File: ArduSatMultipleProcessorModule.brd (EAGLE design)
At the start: 95.5 x 90.3 mm, 95 parts, among them IC1 ATMEGA328P, IC2 ATMEGA328P, IC3 ATMEGA328P, IC4 ATMEGA328P, IC5 MCP23017SO, IC6 MCP23017SO, IC7 ATMEGA328P, P1 N1_ICSP, P2 N0_ICSP, P3 N0_ICSP, P4 N1_ICSP, P5 N1_ICSP, Q1 BSS138 N-MOSFET, Q10 2N7002 N-MOSFET, Q2 BSS138 N-MOSFET, Q3 BSS138 N-MOSFET, Q4 BSS138 N-MOSFET, Q5 BSS138 N-MOSFET, Q6 BSS138 N-MOSFET, Q7 BSS138 N-MOSFET, Q8 BSS138 N-MOSFET, Q9 2N7002 N-MOSFET, U1 MUX-74HC4067, U2 MUX-74HC4067, U3 MUX-74HC4067, U4 MUX-74HC4067

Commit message: Supervisor now has control of both node power and serial comms
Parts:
- removed U1, U2, U3, U4: MUX-74HC4067, SparkFun:SSOP24
- added IC8: MCP23S17ML, freetronics-jon:QFN28-ML_6X6MM
- added U$57, U$58, U$59, U$60: MUX-74HC4067-QFNSMT, freetronics-jon:DHVQFN24
- IC5, IC6: value MCP23017SO -> MCP23017ML; device microchip:SO28W -> freetronics-jon:QFN28-ML_6X6MM
- moved C15 293.1 mm to (65.4, 48.9)
- moved JP3 293.1 mm to (69.2, 55.9)
- moved Q10 293.1 mm to (65.4, 52.1)
- moved Q9 293.1 mm to (65.4, 56.5)
- moved C13 238.7 mm to (36.8, 31.1)
- moved C14 238.7 mm to (41.3, 31.1)
- moved IC7 238.7 mm to (38.7, 47.6)
- moved JP2 238.7 mm to (40.0, 57.8)
- moved P5 238.7 mm to (40.0, 37.5)
- moved R20 238.7 mm to (45.7, 61.6)
- moved R22 238.7 mm to (48.9, 61.6)
- moved R23 238.7 mm to (52.1, 61.6)
- moved R24 238.7 mm to (55.2, 61.6)
- moved R25 238.7 mm to (36.8, 54.0)
- moved R26 238.7 mm to (45.7, 31.1)
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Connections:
- net S_D0_N2_PWR renamed S_D0
- net S_D1_N3_PWR renamed S_D1
- net S_D2_N4_PWR renamed S_D2
- net S_D3_N5_PWR renamed S_D3
- net S_D4_N6_PWR renamed S_D4
- removed net N10_5V: IC6.3
- removed net N11_5V: IC6.4
- removed net N12_5V: IC6.5
- removed net N13_5V: IC6.6
- removed net N14_5V: IC6.7
- removed net N15_5V: IC6.8
- removed net N4_5V: IC6.25
- removed net N5_5V: IC6.26
- removed net N6_5V: IC6.27
- removed net N7_5V: IC6.28
- removed net N8_5V: IC6.1
- removed net N9_5V: IC6.2
- removed net S_A6_N0_PWR: IC7.19, Q9.1
- removed net S_A7_N1_PWR: IC7.22, Q10.1
- new net N$90: IC8.14
- new net N0_PWR: IC6.17, IC8.17, Q9.1
- new net N10_PWR: IC6.27, IC8.27
- new net N11_PWR: IC6.28, IC8.28
- new net N12_PWR: IC6.1, IC8.1
- new net N13_PWR: IC6.2, IC8.2
- new net N14_PWR: IC6.3, IC8.3
- new net N15_PWR: IC6.4, IC8.4
- new net N1_PWR: IC6.18, IC8.18, Q10.1
- new net N2_PWR: IC6.19, IC8.19
- new net N3_PWR: IC6.20, IC8.20
- new net N4_PWR: IC6.21, IC8.21
- new net N5_PWR: IC6.22, IC8.22
- new net N6_PWR: IC6.23, IC8.23
- new net N7_PWR: IC6.24, IC8.24
- new net N8_PWR: IC6.25, IC8.25
- new net N9_PWR: IC6.26, IC8.26
- new net S_A6: IC7.19, R33.1, U$59.15, U$60.15
- new net S_A7: IC7.22
- net +5V_SYS: now also IC5.5, IC6.5, IC8.5, R33.2, U$57.24, U$57.25, U$58.24, U$58.25, U$59.24, U$59.25, U$60.24, U$60.25; no longer IC5.9, IC6.9, U1.24, U2.24, U3.24, U4.24
- net ADDR0: now also IC5.11; no longer IC5.15
- net ADDR1: now also IC5.12; no longer IC5.16
- net ADDR2: now also IC5.13; no longer IC5.17
- net GND: now also IC5.6, IC6.6, IC8.11, IC8.12, IC8.13, IC8.6, U$57.12, U$58.12, U$59.12, U$60.12; no longer IC5.10, IC6.10, R33.1, U1.12, U2.12, U3.12, U4.12
- net N0_5V: no longer IC6.21
- net N0_D0_RX: now also U$58.9, U$59.9; no longer U2.9, U4.9
- net N0_D1_TX: now also U$57.9, U$60.9; no longer U1.9, U3.9
- net N10_D0_RX: now also U$58.21, U$59.21; no longer U2.21, U4.21
- net N10_D1_TX: now also U$57.21, U$60.21; no longer U1.21, U3.21
- net N11_D0_RX: now also U$58.20, U$59.20; no longer U2.20, U4.20
- net N11_D1_TX: now also U$57.20, U$60.20; no longer U1.20, U3.20
- net N12_D0_RX: now also U$58.19, U$59.19; no longer U2.19, U4.19
- net N12_D1_TX: now also U$57.19, U$60.19; no longer U1.19, U3.19
- net N13_D0_RX: now also U$58.18, U$59.18; no longer U2.18, U4.18
- net N13_D1_TX: now also U$57.18, U$60.18; no longer U1.18, U3.18
- net N14_D0_RX: now also U$58.17, U$59.17; no longer U2.17, U4.17
- net N14_D1_TX: now also U$57.17, U$60.17; no longer U1.17, U3.17
- net N15_D0_RX: now also U$58.16, U$59.16; no longer U2.16, U4.16
- net N15_D1_TX: now also U$57.16, U$60.16; no longer U1.16, U3.16
- net N1_5V: no longer IC6.22
- net N1_D0_RX: now also U$58.8, U$59.8; no longer U2.8, U4.8
- net N1_D1_TX: now also U$57.8, U$60.8; no longer U1.8, U3.8
- net N2_5V: no longer IC6.23
- net N2_D0_RX: now also U$58.7, U$59.7; no longer U2.7, U4.7
- net N2_D1_TX: now also U$57.7, U$60.7; no longer U1.7, U3.7
- net N3_5V: no longer IC6.24
- net N3_D0_RX: now also U$58.6, U$59.6; no longer U2.6, U4.6
- net N3_D1_TX: now also U$57.6, U$60.6; no longer U1.6, U3.6
- net N4_D0_RX: now also U$58.5, U$59.5; no longer U2.5, U4.5
- net N4_D1_TX: now also U$57.5, U$60.5; no longer U1.5, U3.5
- net N5_D0_RX: now also U$58.4, U$59.4; no longer U2.4, U4.4
- net N5_D1_TX: now also U$57.4, U$60.4; no longer U1.4, U3.4
- net N6_D0_RX: now also U$58.3, U$59.3; no longer U2.3, U4.3
- net N6_D1_TX: now also U$57.3, U$60.3; no longer U1.3, U3.3
- net N7_D0_RX: now also U$58.2, U$59.2; no longer U2.2, U4.2
- net N7_D1_TX: now also U$57.2, U$60.2; no longer U1.2, U3.2
- net N8_D0_RX: now also U$58.23, U$59.23; no longer U2.23, U4.23
- net N8_D1_TX: now also U$57.23, U$60.23; no longer U1.23, U3.23
- net N9_D0_RX: now also U$58.22, U$59.22; no longer U2.22, U4.22
- net N9_D1_TX: now also U$57.22, U$60.22; no longer U1.22, U3.22
- net PWR_ADDR0: now also IC6.11; no longer IC6.15
- net PWR_ADDR1: now also IC6.12; no longer IC6.16
- net PWR_ADDR2: now also IC6.13; no longer IC6.17
- net RESET: now also IC5.14, IC6.14; no longer IC5.18, IC6.18
- net RX: now also U$58.1, U$59.1; no longer U2.1, U4.1
- net S_A0: now also IC5.17, U$57.10, U$58.10, U$59.10, U$60.10; no longer IC5.21, U1.10, U2.10, U3.10, U4.10
- net S_A1: now also IC5.18, U$57.11, U$58.11, U$59.11, U$60.11; no longer IC5.22, U1.11, U2.11, U3.11, U4.11
- net S_A2: now also IC5.19, U$57.14, U$58.14, U$59.14, U$60.14; no longer IC5.23, U1.14, U2.14, U3.14, U4.14
- net S_A3: now also IC5.20, U$57.13, U$58.13, U$59.13, U$60.13; no longer IC5.24, U1.13, U2.13, U3.13, U4.13
- net S_A4_SDA: now also IC5.9, IC6.9; no longer IC5.13, IC6.13
- net S_A5_SCL: now also IC5.8, IC6.8; no longer IC5.12, IC6.12
- net S_D10: now also IC8.7
- net S_D11_MOSI: now also IC8.9
- net S_D12_MISO: now also IC8.10
- net S_D13_SCK: now also IC8.8
- net TX: now also U$57.1, U$60.1; no longer U1.1, U3.1
- net UART_EN: now also U$57.15, U$58.15; no longer R33.2, U1.15, U2.15, U3.15, U4.15

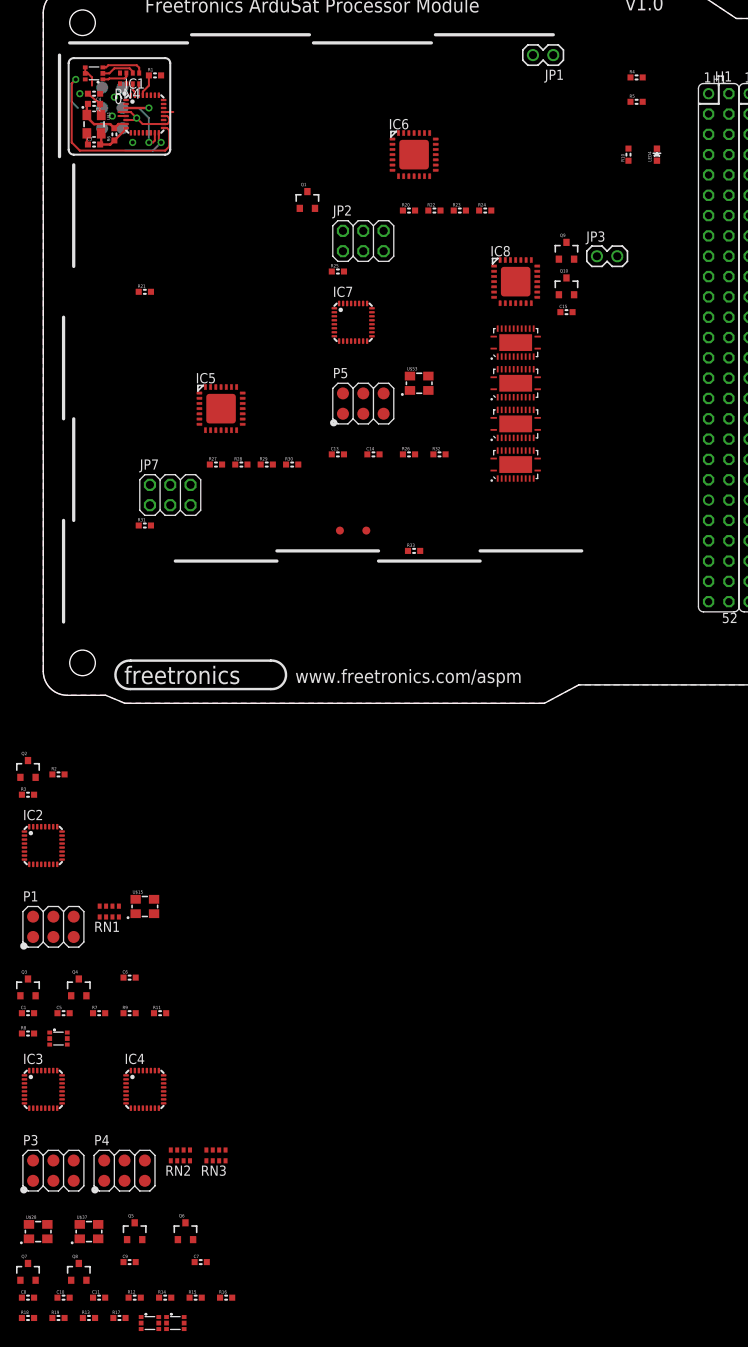
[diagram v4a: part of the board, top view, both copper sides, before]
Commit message: Removed direct control option for UART MUX and power
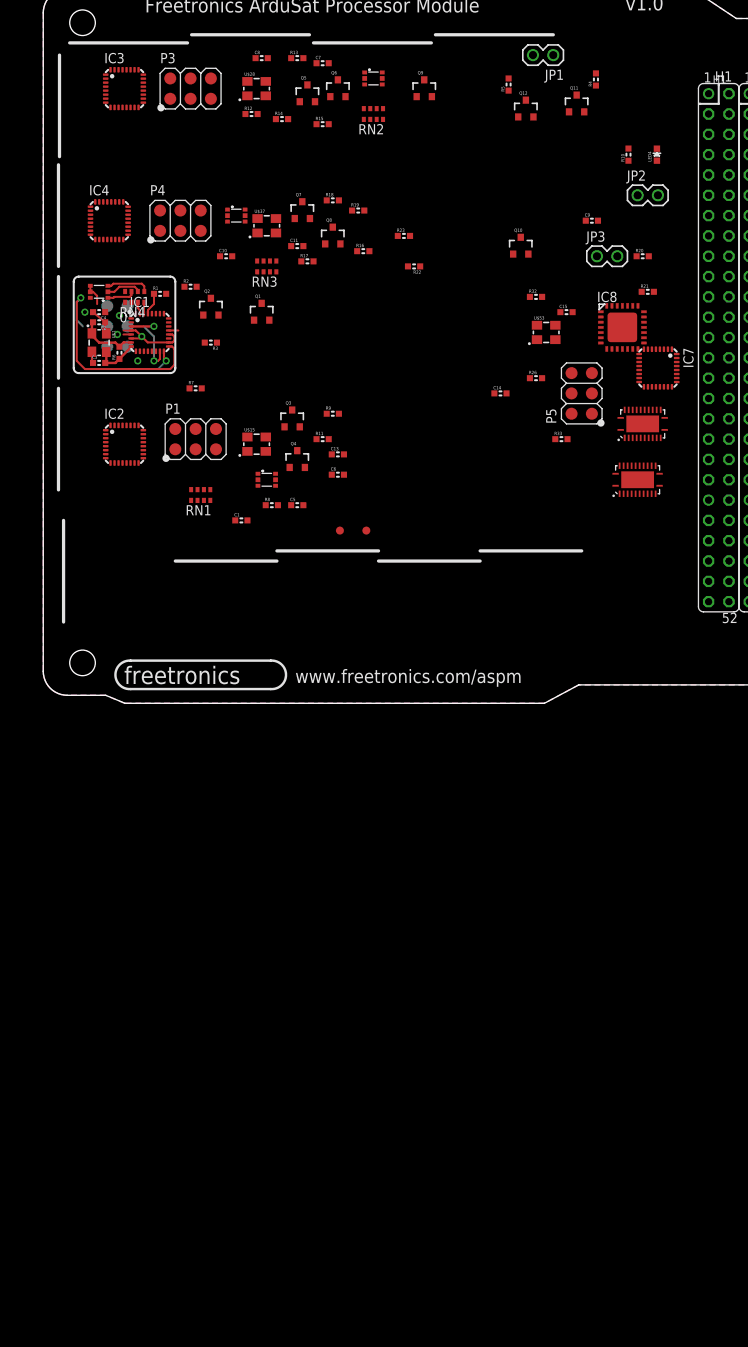
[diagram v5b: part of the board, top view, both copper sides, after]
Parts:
- removed IC5, IC6: MCP23017ML, freetronics-jon:QFN28-ML_6X6MM
- removed JP7: (no value), freetronics-master-v1.1:2X03
- removed R24, R25, R27, R28: 4K7, freetronics-master-v1:0603
- removed R29, R30, R31: 33K, freetronics-master-v1:0603
- removed U$57, U$58: MUX-74HC4067-QFNSMT, freetronics-jon:DHVQFN24
- added Q11, Q12: BSS138 N-MOSFET, freetronics-master-v1:SOT23-3
- JP2: device freetronics-master-v1.1:2X03 -> freetronics-master-v1.1:1X02
- R20: value 33K -> 100K 0603; device freetronics-master-v1:0603 -> freetronics-master-v1.1:0603
- R21: value 33K 0603 -> 100K 0603
- R22, R23: value 33K -> 10K 0603; device freetronics-master-v1:0603 -> freetronics-master-v1.1:0603
- moved R13 159.6 mm to (31.8, 80.6)
- moved U$29 158.1 mm to (41.3, 78.1)
- moved C8 157.7 mm to (27.3, 80.6)
- moved C7 150.6 mm to (34.9, 80.0)
- moved R12 148.7 mm to (26.0, 73.7)
- moved R14 148.0 mm to (29.8, 73.0)
- moved R15 147.5 mm to (34.9, 72.4)
- moved U$28 145.5 mm to (26.7, 76.8)
- moved R18 144.8 mm to (36.2, 62.9)
- moved Q6 144.1 mm to (36.8, 76.8)
- moved Q5 143.9 mm to (33.0, 76.2)
- moved R19 143.4 mm to (39.4, 61.6)
- moved C9 142.4 mm to (68.6, 60.3)
- moved U$38 138.6 mm to (24.1, 61.0)
- moved Q7 137.1 mm to (32.4, 61.6)
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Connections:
- removed net ADDR0: IC5.11, JP7.2, R29.2
- removed net ADDR1: IC5.12, JP7.4, R30.2
- removed net ADDR2: IC5.13, JP7.6, R31.2
- removed net PWR_ADDR0: IC6.11, JP2.2, R20.2
- removed net PWR_ADDR1: IC6.12, JP2.4, R22.2
- removed net PWR_ADDR2: IC6.13, JP2.6, R23.2
- removed net RESET: IC5.14, IC6.14
- removed net SCL: JP1.2, Q2.3, Q4.3, Q6.3, Q8.3, R5.1
- removed net SDA: JP1.1, Q1.3, Q3.3, Q5.3, Q7.3, R4.1
- removed net UART_EN: R21.2, U$57.15, U$58.15
- new net MGMNT_SCL: JP1.2, Q12.3, R5.1
- new net MGMNT_SDA: JP1.1, Q11.3, R4.1
- new net NODE_SCL: JP2.2, Q2.3, Q4.3, Q6.3, Q8.3, R21.1
- new net NODE_SDA: JP2.1, Q1.3, Q3.3, Q5.3, Q7.3, R20.1
- net +5V_SYS: now also R20.2, R21.2; no longer IC5.5, IC6.5, JP2.1, JP2.3, JP2.5, JP7.1, JP7.3, JP7.5, R24.2, R25.2, R27.2, R28.2, U$57.24, U$57.25, U$58.24, U$58.25
- net GND: no longer IC5.6, IC6.6, R20.1, R21.1, R22.1, R23.1, R29.1, R30.1, R31.1, U$57.12, U$58.12
- net N0_D0_RX: no longer U$58.9
- net N0_D1_TX: no longer U$57.9
- net N0_PWR: no longer IC6.17
- net N10_D0_RX: no longer U$58.21
- net N10_D1_TX: no longer U$57.21
- net N10_PWR: no longer IC6.27
- net N11_D0_RX: no longer U$58.20
- net N11_D1_TX: no longer U$57.20
- net N11_PWR: no longer IC6.28
- net N12_D0_RX: no longer U$58.19
- net N12_D1_TX: no longer U$57.19
- net N12_PWR: no longer IC6.1
- net N13_D0_RX: no longer U$58.18
- net N13_D1_TX: no longer U$57.18
- net N13_PWR: no longer IC6.2
- net N14_D0_RX: no longer U$58.17
- net N14_D1_TX: no longer U$57.17
- net N14_PWR: no longer IC6.3
- net N15_D0_RX: no longer U$58.16
- net N15_D1_TX: no longer U$57.16
- net N15_PWR: no longer IC6.4
- net N1_5V: now also Q11.1, Q12.1, R22.2, R23.2
- net N1_D0_RX: no longer U$58.8
- net N1_D1_TX: no longer U$57.8
- net N1_PWR: no longer IC6.18
- net N2_D0_RX: no longer U$58.7
- net N2_D1_TX: no longer U$57.7
- net N2_PWR: no longer IC6.19
- net N3_D0_RX: no longer U$58.6
- net N3_D1_TX: no longer U$57.6
- net N3_PWR: no longer IC6.20
- net N4_D0_RX: no longer U$58.5
- net N4_D1_TX: no longer U$57.5
- net N4_PWR: no longer IC6.21
- net N5_D0_RX: no longer U$58.4
- net N5_D1_TX: no longer U$57.4
- net N5_PWR: no longer IC6.22
- net N6_D0_RX: no longer U$58.3
- net N6_D1_TX: no longer U$57.3
- net N6_PWR: no longer IC6.23
- net N7_D0_RX: no longer U$58.2
- net N7_D1_TX: no longer U$57.2
- net N7_PWR: no longer IC6.24
- net N8_D0_RX: no longer U$58.23
- net N8_D1_TX: no longer U$57.23
- net N8_PWR: no longer IC6.25
- net N9_D0_RX: no longer U$58.22
- net N9_D1_TX: no longer U$57.22
- net N9_PWR: no longer IC6.26
- net RX: no longer U$58.1
- net S_A0: no longer IC5.17, U$57.10, U$58.10
- net S_A1: no longer IC5.18, U$57.11, U$58.11
- net S_A2: no longer IC5.19, U$57.14, U$58.14
- net S_A3: no longer IC5.20, U$57.13, U$58.13
- net S_A4_SDA: now also Q11.2, R22.1; no longer IC5.9, IC6.9, R24.1, R28.1
- net S_A5_SCL: now also Q12.2, R23.1; no longer IC5.8, IC6.8, R25.1, R27.1
- net TX: no longer U$57.1

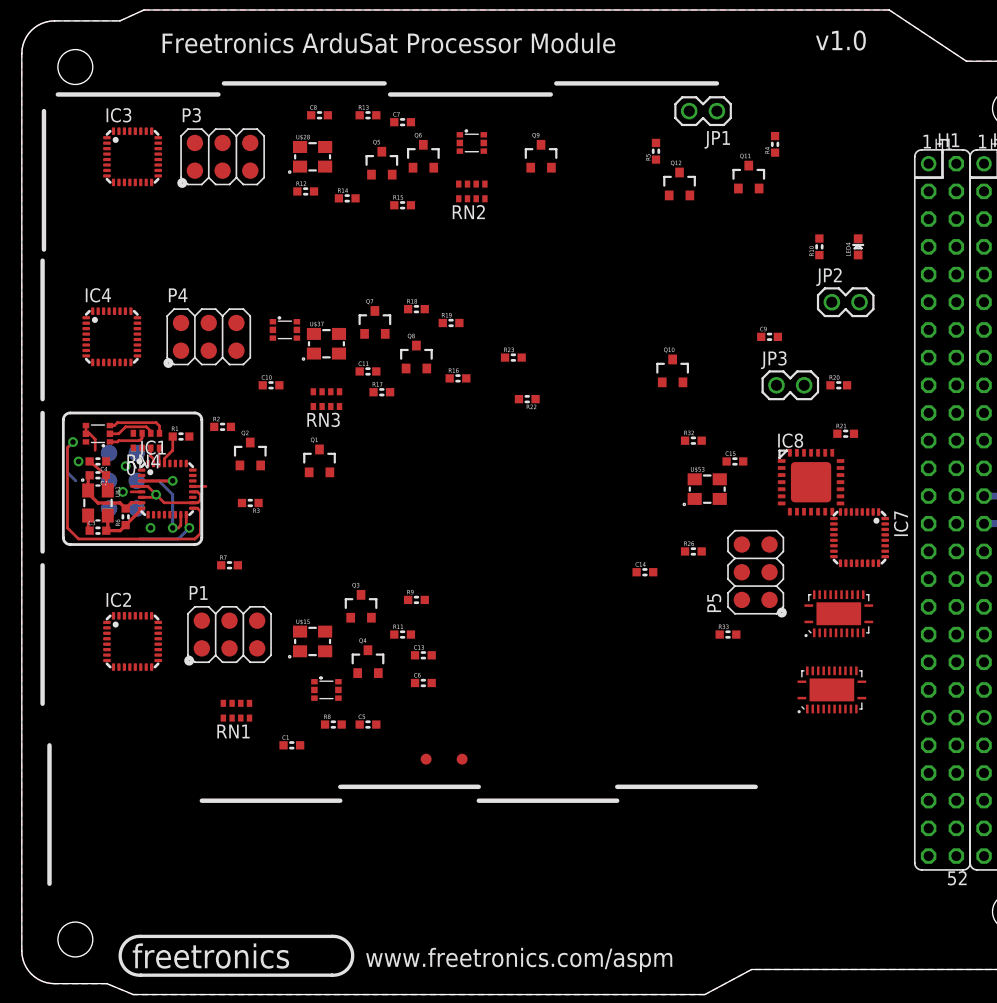
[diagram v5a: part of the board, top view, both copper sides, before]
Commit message: Experiments with node layout
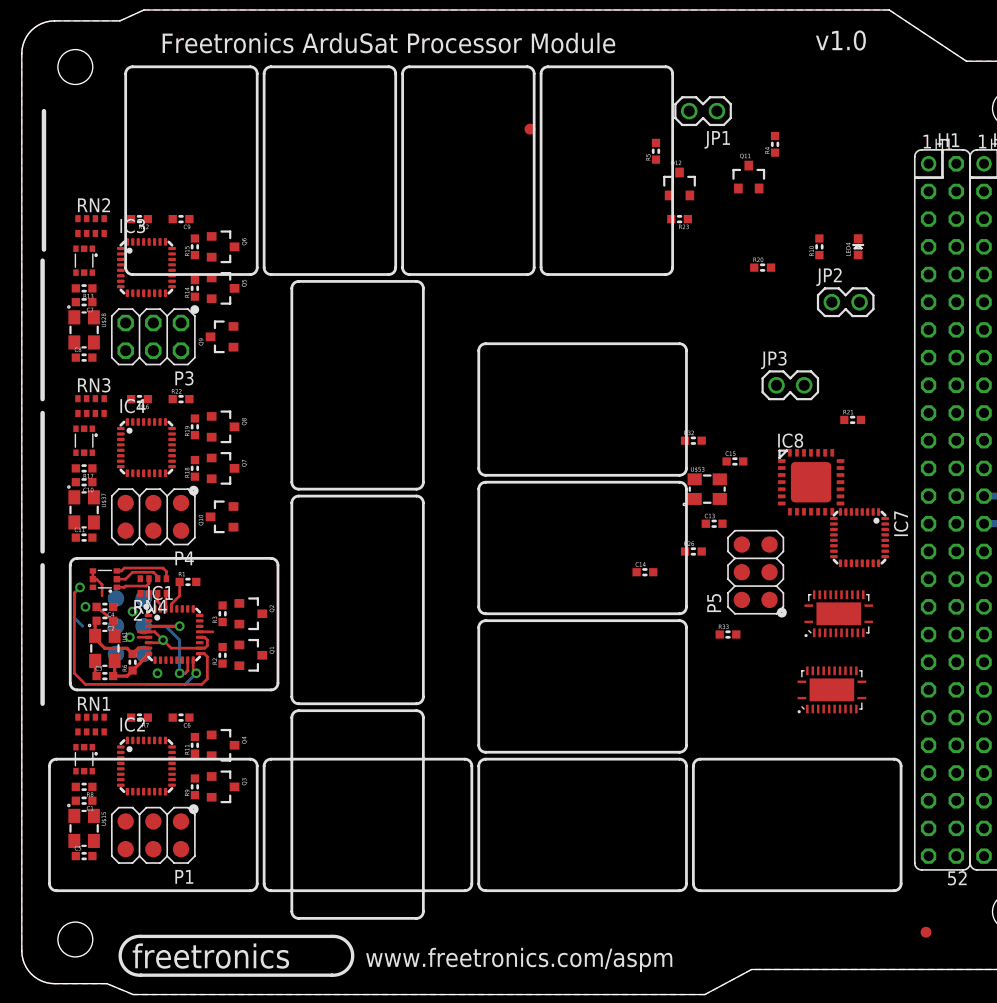
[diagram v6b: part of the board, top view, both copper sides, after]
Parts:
- P3: device freetronics-jon:2X03SURFACE -> freetronics-jon:2X03PTH
- moved U$21 58.6 mm to (46.6, 79.4)
- moved C9 55.0 mm to (14.6, 71.1), turned to 180 degrees
- moved U$22 45.4 mm to (82.9, 5.71)
- moved Q10 43.4 mm to (18.4, 43.8), turned to 90 degrees
- moved U$29 37.2 mm to (5.71, 67.3), turned to 270 degrees
- moved RN2 35.1 mm to (6.35, 70.5), turned to 180 degrees
- moved C7 33.6 mm to (5.71, 63.5), turned to 180 degrees
- moved Q9 33.6 mm to (18.4, 60.3), turned to 90 degrees
- moved R22 31.7 mm to (14.6, 54.6), turned to 0 degrees
- moved C8 31.0 mm to (5.71, 58.4)
- moved R13 30.5 mm to (5.71, 64.8), turned to 180 degrees
- moved C11 30.2 mm to (5.71, 41.9)
- moved R16 29.3 mm to (10.8, 54.6), turned to 180 degrees
- moved C13 29.3 mm to (63.5, 43.2)
- moved C5 28.7 mm to (5.71, 12.7)
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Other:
- board text added: "2"
- board text removed: "0"

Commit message: Experiments in node dimensions and layout
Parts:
- P4: device freetronics-jon:2X03SURFACE -> freetronics-jon:2X03PTH
- moved U$59 77.8 mm to (10.2, 78.1)
- moved U$60 74.6 mm to (19.7, 78.7)
- moved IC7 54.0 mm to (36.2, 77.5)
- moved IC8 53.9 mm to (27.9, 77.5)
- moved C15 46.0 mm to (19.6, 45.2)
- moved P5 42.2 mm to (52.1, 78.1)
- moved R22 41.6 mm to (52.6, 71.6), turned to 180 degrees
- moved R33 39.4 mm to (63.5, 72.4)
- moved JP2 38.6 mm to (40.0, 81.3)
- moved U$53 37.4 mm to (41.3, 76.8)
- moved C13 35.1 mm to (71.1, 77.5)
- moved C14 34.7 mm to (52.1, 73.0)
- moved R26 32.2 mm to (56.5, 72.4)
- moved JP3 31.0 mm to (43.8, 73.7)
- moved R21 27.1 mm to (71.1, 79.4)
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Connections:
- net +5V_SYS: now also Q11.1, Q12.1, R22.2, R23.2
- net GND: now also RN3.1; no longer RN3.2
- net N$19: now also U$38.3; no longer U$38.2
- net N$20: now also RN3.7, U$38.2; no longer RN3.5, U$38.3
- net N$21: now also RN3.8; no longer RN3.7
- net N1_5V: no longer Q11.1, Q12.1, R22.2, R23.2
- net N1_D0_RX: now also RN3.3; no longer RN3.4
- net N1_D1_TX: now also RN3.2; no longer RN3.3
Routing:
- net N1_5V: track 0.00 -> 42.2 mm
- net N1_D13_SCK: track 0.00 -> 17.5 mm, vias 0 -> 2
- net N1_RESET: track 0.00 -> 14.8 mm, vias 0 -> 1
- net GND: track 10.2 -> 22.9 mm, vias 5 -> 10
- net N$17: track 0.00 -> 10.8 mm
- net N1_A4_SDA: track 0.00 -> 8.53 mm
- net N$18: track 0.00 -> 8.18 mm
- net N1_A5_SCL: track 0.00 -> 7.44 mm
- net N1_D11_MOSI: track 0.00 -> 5.80 mm
- net N2_D13_SCK: track 27.9 -> 33.4 mm
- net N1_D0_RX: track 0.00 -> 5.21 mm, vias 0 -> 1
- net N$19: track 0.00 -> 4.04 mm
- net N1_D1_TX: track 0.00 -> 3.31 mm, vias 0 -> 1
- net N1_D12_MISO: track 0.00 -> 3.00 mm
- net N$20: track 0.00 -> 2.80 mm
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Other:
- board text added: "0"
- board text added: "1"
- board text added: "3"
- board text added: "4"
- board text added: "5"
- board text added: "6"
- board text added: "7"
- board text added: "9"
- board text added: "Freetronics ArduSat Multiple Processor Module"
- board text removed: "Freetronics ArduSat Processor Module"
